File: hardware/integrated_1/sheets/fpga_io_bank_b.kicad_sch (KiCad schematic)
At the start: 6 parts, among them U1 XC6SLX9-TQG144

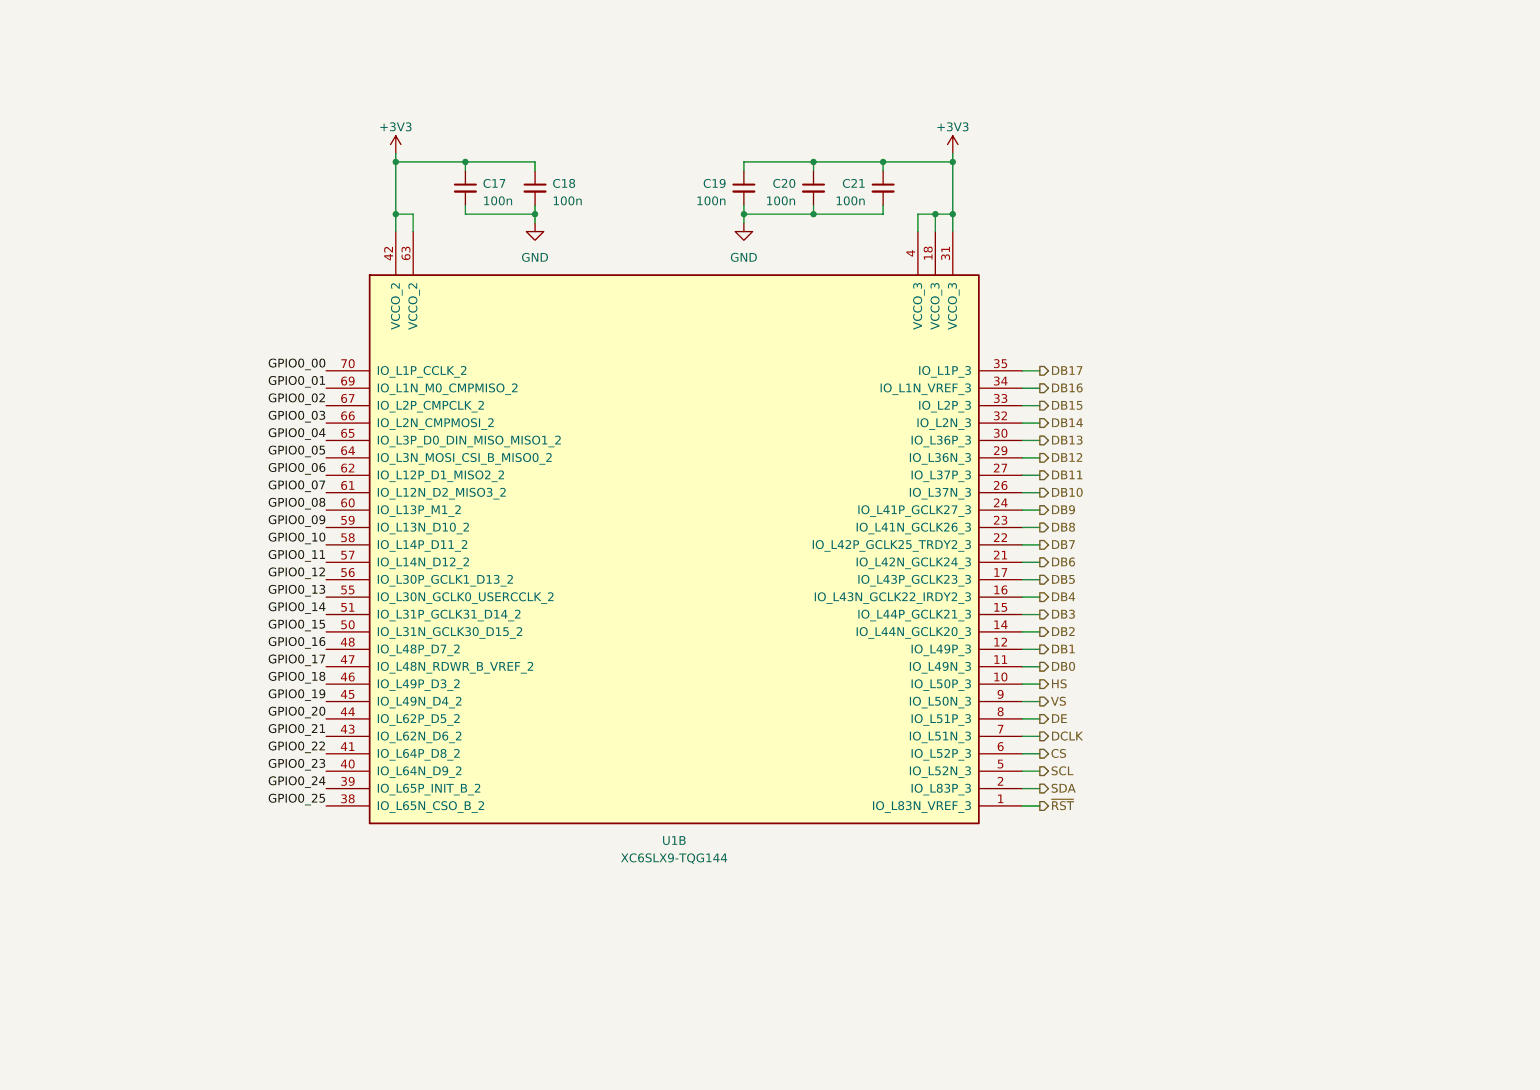
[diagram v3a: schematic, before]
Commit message: added leds
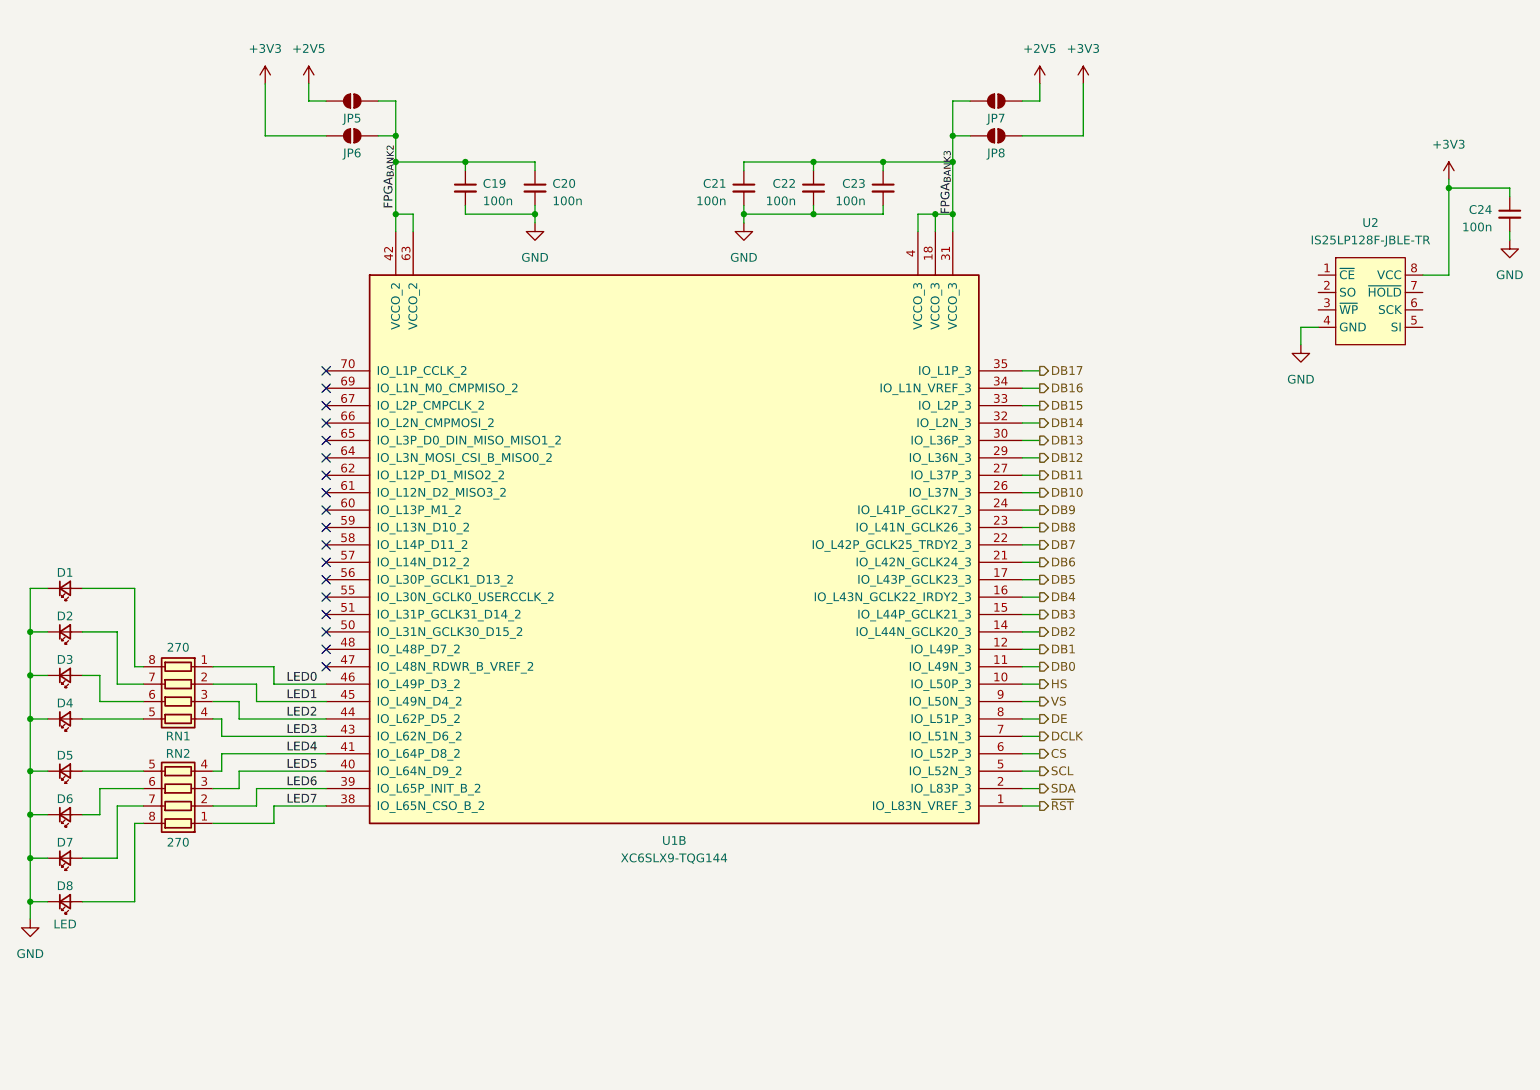
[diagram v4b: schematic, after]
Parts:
- added C24: 100n, KiCAD Library:C_0402_1005Metric, symbol Device:C_Small
- added D1, D2, D3, D4, D5, D6, D7, D8: LED, KiCAD Library:D_0805_2012Metric, symbol Device:LED_Small
- added JP5, JP6, JP7, JP8: SolderJumper_2_Open, Jumper:SolderJumper-2_P1.3mm_Open_RoundedPad1.0x1.5mm, symbol Jumper:SolderJumper_2_Open
- added RN1, RN2: 270, KiCAD Library:C_ARRAY_EXB28V_PAN-L, symbol Device:R_Pack04
- added U2: IS25LP128F-JBLE-TR, Package_SO:SOIC-8_5.275x5.275mm_P1.27mm, symbol Cuprum:IS25LP128F-JBLE-TR
- renumbered C17 to C19, C18 to C20, C19 to C21, C20 to C22, C21 to C23
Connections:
- net +3V3: now also C24.1, JP6.1 (A), JP8.1 (A), U2.8 (VCC); no longer C19.1, C20.1, C21.1, C22.1, C23.1, U1.18 (VCCO_3), U1.31 (VCCO_3), U1.4 (VCCO_3), U1.42 (VCCO_2), U1.63 (VCCO_2)
- net GND: now also C24.2, D1.1 (K), D2.1 (K), D3.1 (K), D4.1 (K), D5.1 (K), D6.1 (K), D7.1 (K), D8.1 (K), U2.4 (GND)
- net GPIO0_00: no longer names the net of U1.70 (IO_L1P_CCLK_2)
- net GPIO0_01: no longer names the net of U1.69 (IO_L1N_M0_CMPMISO_2)
- net GPIO0_02: no longer names the net of U1.67 (IO_L2P_CMPCLK_2)
- net GPIO0_03: no longer names the net of U1.66 (IO_L2N_CMPMOSI_2)
- net GPIO0_04: no longer names the net of U1.65 (IO_L3P_D0_DIN_MISO_MISO1_2)
- net GPIO0_05: no longer names the net of U1.64 (IO_L3N_MOSI_CSI_B_MISO0_2)
- net GPIO0_06: no longer names the net of U1.62 (IO_L12P_D1_MISO2_2)
- net GPIO0_07: no longer names the net of U1.61 (IO_L12N_D2_MISO3_2)
- net GPIO0_08: no longer names the net of U1.60 (IO_L13P_M1_2)
- net GPIO0_09: no longer names the net of U1.59 (IO_L13N_D10_2)
- net GPIO0_10: no longer names the net of U1.58 (IO_L14P_D11_2)
- net GPIO0_11: no longer names the net of U1.57 (IO_L14N_D12_2)
- net GPIO0_12: no longer names the net of U1.56 (IO_L30P_GCLK1_D13_2)
- net GPIO0_13: no longer names the net of U1.55 (IO_L30N_GCLK0_USERCCLK_2)
- net GPIO0_14: no longer names the net of U1.51 (IO_L31P_GCLK31_D14_2)
- net GPIO0_15: no longer names the net of U1.50 (IO_L31N_GCLK30_D15_2)
- net GPIO0_16: no longer names the net of U1.48 (IO_L48P_D7_2)
- net GPIO0_17: no longer names the net of U1.47 (IO_L48N_RDWR_B_VREF_2)
- net GPIO0_18 renamed LED0
- net LED0: now also RN1.1 (R1.1)
- net GPIO0_19 renamed LED1
- net LED1: now also RN1.2 (R2.1)
- net GPIO0_20 renamed LED2
- net LED2: now also RN1.3 (R3.1)
- net GPIO0_21 renamed LED3
- net LED3: now also RN1.4 (R4.1)
- net GPIO0_22 renamed LED4
- net LED4: now also RN2.4 (R4.1)
- net GPIO0_23 renamed LED5
- net LED5: now also RN2.3 (R3.1)
- net GPIO0_24 renamed LED6
- net LED6: now also RN2.2 (R2.1)
- net GPIO0_25 renamed LED7
- net LED7: now also RN2.1 (R1.1)
- new net: D1.2 (A), RN1.8 (R1.2)
- new net: D7.2 (A), RN2.7 (R2.2)
- new net: D4.2 (A), RN1.5 (R4.2)
- new net: D3.2 (A), RN1.6 (R3.2)
- new net: D2.2 (A), RN1.7 (R2.2)
- new net: D8.2 (A), RN2.8 (R1.2)
- new net: D6.2 (A), RN2.6 (R3.2)
- new net: D5.2 (A), RN2.5 (R4.2)
- new net +2V5: JP5.1 (A), JP7.1 (A)
- new net FPGA_{BANK2}: C19.1, C20.1, JP5.2 (B), JP6.2 (B), U1.42 (VCCO_2), U1.63 (VCCO_2)
- new net FPGA_{BANK3}: C21.1, C22.1, C23.1, JP7.2 (B), JP8.2 (B), U1.18 (VCCO_3), U1.31 (VCCO_3), U1.4 (VCCO_3)
- no-connect marks 0 -> 18

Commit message: finalizing the schematic and layout
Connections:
- net LED0: now also U1.47 (IO_L48N_RDWR_B_VREF_2); no longer U1.46 (IO_L49P_D3_2)
- net LED1: now also U1.46 (IO_L49P_D3_2); no longer U1.45 (IO_L49N_D4_2)
- net LED2: now also U1.45 (IO_L49N_D4_2); no longer U1.44 (IO_L62P_D5_2)
- net LED3: now also U1.44 (IO_L62P_D5_2); no longer U1.43 (IO_L62N_D6_2)
- net LED4: now also U1.43 (IO_L62N_D6_2); no longer U1.41 (IO_L64P_D8_2)
- net LED5: now also U1.41 (IO_L64P_D8_2); no longer U1.40 (IO_L64N_D9_2)
- net LED6: now also U1.40 (IO_L64N_D9_2); no longer U1.39 (IO_L65P_INIT_B_2)
- net LED7: now also U1.39 (IO_L65P_INIT_B_2); no longer U1.38 (IO_L65N_CSO_B_2)
- net ~{CS}: now reaches U2.1 (~{CE})
- net ~{CS}: now also U1.38 (IO_L65N_CSO_B_2)
- net D_{1}: now reaches U2.2 (SO)
- net D_{1}: now also U1.65 (IO_L3P_D0_DIN_MISO_MISO1_2)
- net D_{2}: now reaches U2.3 (~{WP})
- net D_{2}: now also U1.62 (IO_L12P_D1_MISO2_2)
- net D_{0}: now reaches U2.5 (SI)
- net D_{0}: now also U1.64 (IO_L3N_MOSI_CSI_B_MISO0_2)
- net CLK: now reaches U2.6 (SCK)
- net CLK: now also U1.70 (IO_L1P_CCLK_2)
- net D_{3}: now reaches U2.7 (~{HOLD})
- net D_{3}: now also U1.61 (IO_L12N_D2_MISO3_2)
- no-connect marks 18 -> 10
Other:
- moved on the sheet: C19, C20, C21, C22, C23, C24, D1, D2, D3, D4, D5, D6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

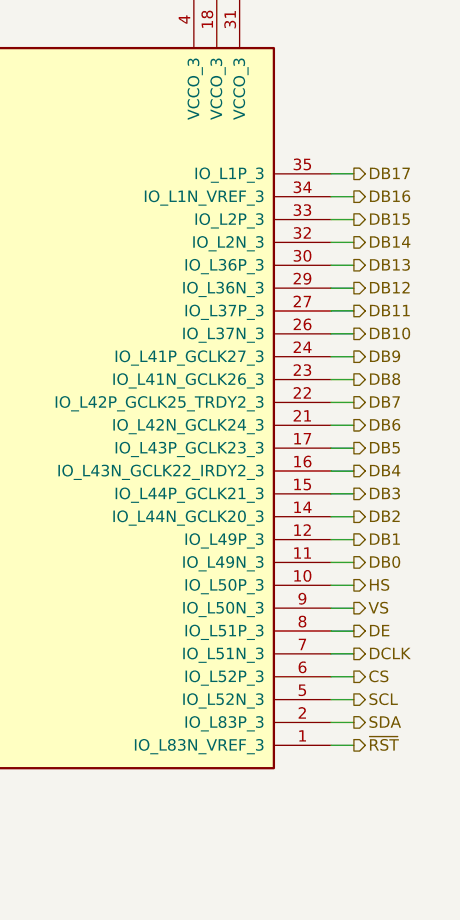
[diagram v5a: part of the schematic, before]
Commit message: fixed critical issue - display connector was mirrored
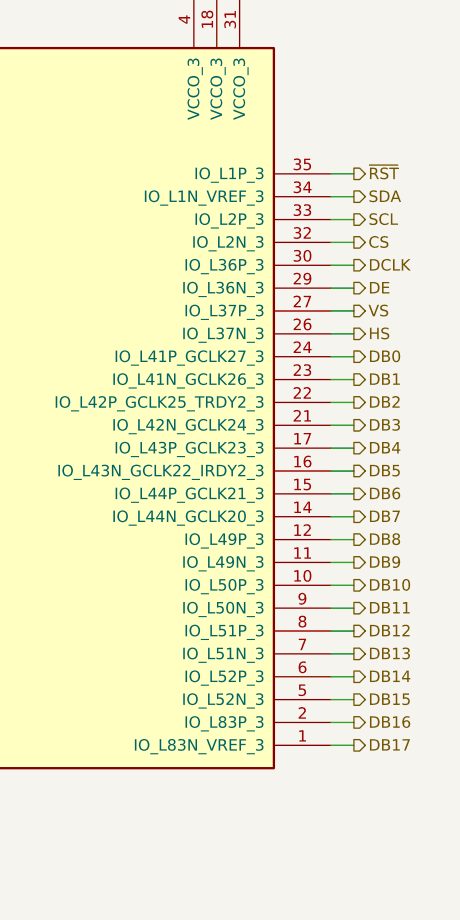
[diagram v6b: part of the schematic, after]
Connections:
- net CS: now also U1.32 (IO_L2N_3); no longer U1.6 (IO_L52P_3)
- net DB0: now also U1.24 (IO_L41P_GCLK27_3); no longer U1.11 (IO_L49N_3)
- net DB1: now also U1.23 (IO_L41N_GCLK26_3); no longer U1.12 (IO_L49P_3)
- net DB10: now also U1.10 (IO_L50P_3); no longer U1.26 (IO_L37N_3)
- net DB11: now also U1.9 (IO_L50N_3); no longer U1.27 (IO_L37P_3)
- net DB12: now also U1.8 (IO_L51P_3); no longer U1.29 (IO_L36N_3)
- net DB13: now also U1.7 (IO_L51N_3); no longer U1.30 (IO_L36P_3)
- net DB14: now also U1.6 (IO_L52P_3); no longer U1.32 (IO_L2N_3)
- net DB15: now also U1.5 (IO_L52N_3); no longer U1.33 (IO_L2P_3)
- net DB16: now also U1.2 (IO_L83P_3); no longer U1.34 (IO_L1N_VREF_3)
- net DB17: now also U1.1 (IO_L83N_VREF_3); no longer U1.35 (IO_L1P_3)
- net DB2: now also U1.22 (IO_L42P_GCLK25_TRDY2_3); no longer U1.14 (IO_L44N_GCLK20_3)
- net DB3: now also U1.21 (IO_L42N_GCLK24_3); no longer U1.15 (IO_L44P_GCLK21_3)
- net DB4: now also U1.17 (IO_L43P_GCLK23_3); no longer U1.16 (IO_L43N_GCLK22_IRDY2_3)
- net DB5: now also U1.16 (IO_L43N_GCLK22_IRDY2_3); no longer U1.17 (IO_L43P_GCLK23_3)
- net DB6: now also U1.15 (IO_L44P_GCLK21_3); no longer U1.21 (IO_L42N_GCLK24_3)
- net DB7: now also U1.14 (IO_L44N_GCLK20_3); no longer U1.22 (IO_L42P_GCLK25_TRDY2_3)
- net DB8: now also U1.12 (IO_L49P_3); no longer U1.23 (IO_L41N_GCLK26_3)
- net DB9: now also U1.11 (IO_L49N_3); no longer U1.24 (IO_L41P_GCLK27_3)
- net DCLK: now also U1.30 (IO_L36P_3); no longer U1.7 (IO_L51N_3)
- net DE: now also U1.29 (IO_L36N_3); no longer U1.8 (IO_L51P_3)
- net HS: now also U1.26 (IO_L37N_3); no longer U1.10 (IO_L50P_3)
- net SCL: now also U1.33 (IO_L2P_3); no longer U1.5 (IO_L52N_3)
- net SDA: now also U1.34 (IO_L1N_VREF_3); no longer U1.2 (IO_L83P_3)
- net VS: now also U1.27 (IO_L37P_3); no longer U1.9 (IO_L50N_3)
- net ~{RST}: now also U1.35 (IO_L1P_3); no longer U1.1 (IO_L83N_VREF_3)
